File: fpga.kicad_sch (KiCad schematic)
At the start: 33 parts, among them Q1 BSS138PW, SW1 SW_B3U-1000P_SMD, U1 ICE40UP5K-SG48, U3 W25Q32JW_SOIC-8

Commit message: [#72447] Unify capacitors
Signed-off-by: Dawid Lentka <dlentka@antmicro.com>
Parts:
- C1, C2, C3, C4, C5, C6: value C_10u_10V_0402 -> C_10u_0402; symbol antmicroCapacitors0402:C_10u_10V_0402 -> antmicroCapacitors0402:C_10u_0402; MPN GRM155R61A106ME11D -> CC0402MRX5R5BB106; Manufacturer Murata -> YAGEO
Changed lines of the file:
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@@
 	)
 	(symbol
-		(lib_id "antmicroCapacitors0402:C_10u_10V_0402")
+		(lib_id "antmicroCapacitors0402:C_10u_0402")
 		(at 43.18 115.57 90)
 		(unit 1)
@@
 			)
 		)
-		(property "Value" "C_10u_10V_0402"
+		(property "Value" "C_10u_0402"
 			(at 53.34 95.25 0)
 			(effects
@@
 			)
 		)
-		(property "Datasheet" "https://www.murata.com/products/productdetail?partno=GRM155R61A106ME11%23"
+		(property "Datasheet" "https://www.yageo.com/en/Chart/Download/pdf/CC0402MRX5R5BB106"
 			(at 58.42 95.25 0)
 			(effects
@@
 			)
 		)
-		(property "Description" "Multilayer Ceramic Capacitors MLCC - SMD/SMT 10 uF 10 VDC 20% 0402 X5R"
+		(property "Description" "SMD Multilayer Ceramic Capacitor, 10 µF, 6.3 V, 0402 [1005 Metric], ± 20%, X5R, CC Series"
 			(at 43.18 115.57 0)
 			(effects
@@
 			)
 		)
-		(property "MPN" "GRM155R61A106ME11D"
+		(property "MPN" "CC0402MRX5R5BB106"
 			(at 60.96 95.25 0)
 			(effects
@@
 			)
 		)
-		(property "Manufacturer" "Murata"
+		(property "Manufacturer" "YAGEO"
 			(at 63.5 95.25 0)
 			(effects
@@
 	)
 	(symbol
-		(lib_id "antmicroCapacitors0402:C_10u_10V_0402")
+		(lib_id "antmicroCapacitors0402:C_10u_0402")
 		(at 43.18 166.37 90)
 		(unit 1)
@@
 			)
 		)
-		(property "Value" "C_10u_10V_0402"
+		(property "Value" "C_10u_0402"
 			(at 53.34 146.05 0)
 			(effects
@@
 			)
 		)
-		(property "Datasheet" "https://www.murata.com/products/productdetail?partno=GRM155R61A106ME11%23"
+		(property "Datasheet" "https://www.yageo.com/en/Chart/Download/pdf/CC0402MRX5R5BB106"
 			(at 58.42 146.05 0)
 			(effects
@@
 			)
 		)
-		(property "Description" "Multilayer Ceramic Capacitors MLCC - SMD/SMT 10 uF 10 VDC 20% 0402 X5R"
+		(property "Description" "SMD Multilayer Ceramic Capacitor, 10 µF, 6.3 V, 0402 [1005 Metric], ± 20%, X5R, CC Series"
 			(at 43.18 166.37 0)
 			(effects
@@
 			)
 		)
-		(property "MPN" "GRM155R61A106ME11D"
+		(property "MPN" "CC0402MRX5R5BB106"
 			(at 60.96 146.05 0)
 			(effects
@@
 			)
 		)
-		(property "Manufacturer" "Murata"
+		(property "Manufacturer" "YAGEO"
 			(at 63.5 146.05 0)
 			(effects
@@
 	)
 	(symbol
-		(lib_id "antmicroCapacitors0402:C_10u_10V_0402")
+		(lib_id "antmicroCapacitors0402:C_10u_0402")
 		(at 43.18 102.87 90)
 		(unit 1)
@@
 			)
 		)
-		(property "Value" "C_10u_10V_0402"
+		(property "Value" "C_10u_0402"
 			(at 53.34 82.55 0)
 			(effects
@@
 			)
 		)
-		(property "Datasheet" "https://www.murata.com/products/productdetail?partno=GRM155R61A106ME11%23"
+		(property "Datasheet" "https://www.yageo.com/en/Chart/Download/pdf/CC0402MRX5R5BB106"
 			(at 58.42 82.55 0)
 			(effects
@@
 			)
 		)
-		(property "Description" "Multilayer Ceramic Capacitors MLCC - SMD/SMT 10 uF 10 VDC 20% 0402 X5R"
+		(property "Description" "SMD Multilayer Ceramic Capacitor, 10 µF, 6.3 V, 0402 [1005 Metric], ± 20%, X5R, CC Series"
 			(at 43.18 102.87 0)
 			(effects
@@
 			)
 		)
-		(property "MPN" "GRM155R61A106ME11D"
+		(property "MPN" "CC0402MRX5R5BB106"
 			(at 60.96 82.55 0)
 			(effects
@@
 			)
 		)
-		(property "Manufacturer" "Murata"
+		(property "Manufacturer" "YAGEO"
 			(at 63.5 82.55 0)
 			(effects
@@
 	)
 	(symbol
-		(lib_id "antmicroCapacitors0402:C_10u_10V_0402")
+		(lib_id "antmicroCapacitors0402:C_10u_0402")
 		(at 43.18 153.67 90)
 		(unit 1)
@@
 			)
 		)
-		(property "Value" "C_10u_10V_0402"
+		(property "Value" "C_10u_0402"
 			(at 53.34 133.35 0)
 			(effects
@@
 			)
 		)
-		(property "Datasheet" "https://www.murata.com/products/productdetail?partno=GRM155R61A106ME11%23"
+		(property "Datasheet" "https://www.yageo.com/en/Chart/Download/pdf/CC0402MRX5R5BB106"
 			(at 58.42 133.35 0)
 			(effects
@@
 			)
 		)
-		(property "Description" "Multilayer Ceramic Capacitors MLCC - SMD/SMT 10 uF 10 VDC 20% 0402 X5R"
+		(property "Description" "SMD Multilayer Ceramic Capacitor, 10 µF, 6.3 V, 0402 [1005 Metric], ± 20%, X5R, CC Series"
 			(at 43.18 153.67 0)
 			(effects
@@
 			)
 		)
-		(property "MPN" "GRM155R61A106ME11D"
+		(property "MPN" "CC0402MRX5R5BB106"
 			(at 60.96 133.35 0)
 			(effects
@@
 			)
 		)
-		(property "Manufacturer" "Murata"
+		(property "Manufacturer" "YAGEO"
 			(at 63.5 133.35 0)
 			(effects
@@
 	)
 	(symbol
-		(lib_id "antmicroCapacitors0402:C_10u_10V_0402")
+		(lib_id "antmicroCapacitors0402:C_10u_0402")
 		(at 43.18 128.27 90)
 		(unit 1)
@@
 			)
 		)
-		(property "Value" "C_10u_10V_0402"
+		(property "Value" "C_10u_0402"
 			(at 53.34 107.95 0)
 			(effects
@@
 			)
 		)
-		(property "Datasheet" "https://www.murata.com/products/productdetail?partno=GRM155R61A106ME11%23"
+		(property "Datasheet" "https://www.yageo.com/en/Chart/Download/pdf/CC0402MRX5R5BB106"
 			(at 58.42 107.95 0)
 			(effects
@@
 			)
 		)
-		(property "Description" "Multilayer Ceramic Capacitors MLCC - SMD/SMT 10 uF 10 VDC 20% 0402 X5R"
+		(property "Description" "SMD Multilayer Ceramic Capacitor, 10 µF, 6.3 V, 0402 [1005 Metric], ± 20%, X5R, CC Series"
 			(at 43.18 128.27 0)
 			(effects
@@
 			)
 		)
-		(property "MPN" "GRM155R61A106ME11D"
+		(property "MPN" "CC0402MRX5R5BB106"
 			(at 60.96 107.95 0)
 			(effects
@@
 			)
 		)
-		(property "Manufacturer" "Murata"
+		(property "Manufacturer" "YAGEO"
 			(at 63.5 107.95 0)
 			(effects
@@
 	)
 	(symbol
-		(lib_id "antmicroCapacitors0402:C_10u_10V_0402")
+		(lib_id "antmicroCapacitors0402:C_10u_0402")
 		(at 43.18 140.97 90)
 		(unit 1)
@@
 			)
 		)
-		(property "Value" "C_10u_10V_0402"
+		(property "Value" "C_10u_0402"
 			(at 53.34 120.65 0)
 			(effects
@@
 			)
 		)
-		(property "Datasheet" "https://www.murata.com/products/productdetail?partno=GRM155R61A106ME11%23"
+		(property "Datasheet" "https://www.yageo.com/en/Chart/Download/pdf/CC0402MRX5R5BB106"
 			(at 58.42 120.65 0)
 			(effects
@@
 			)
 		)
-		(property "Description" "Multilayer Ceramic Capacitors MLCC - SMD/SMT 10 uF 10 VDC 20% 0402 X5R"
+		(property "Description" "SMD Multilayer Ceramic Capacitor, 10 µF, 6.3 V, 0402 [1005 Metric], ± 20%, X5R, CC Series"
 			(at 43.18 140.97 0)
 			(effects
@@
 			)
 		)
-		(property "MPN" "GRM155R61A106ME11D"
+		(property "MPN" "CC0402MRX5R5BB106"
 			(at 60.96 120.65 0)
 			(effects
@@
 			)
 		)
-		(property "Manufacturer" "Murata"
+		(property "Manufacturer" "YAGEO"
 			(at 63.5 120.65 0)
 			(effects

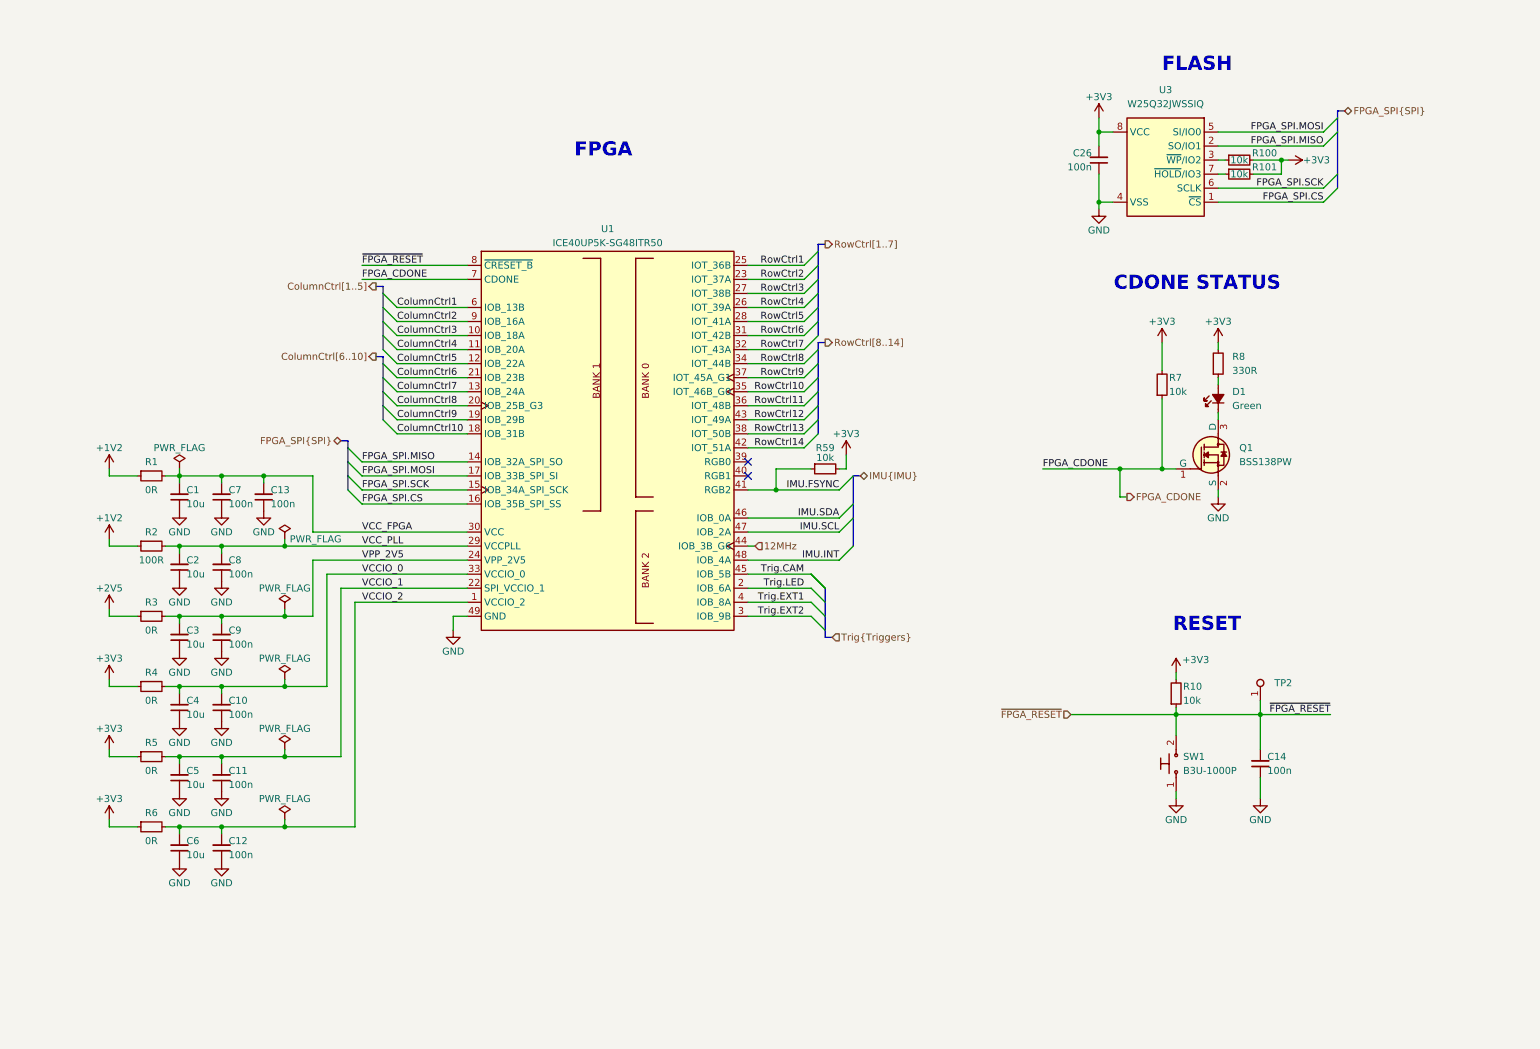
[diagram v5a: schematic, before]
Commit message: [#72447] Update clock & SPI connections
Signed-off-by: Dawid Lentka <dlentka@antmicro.com>
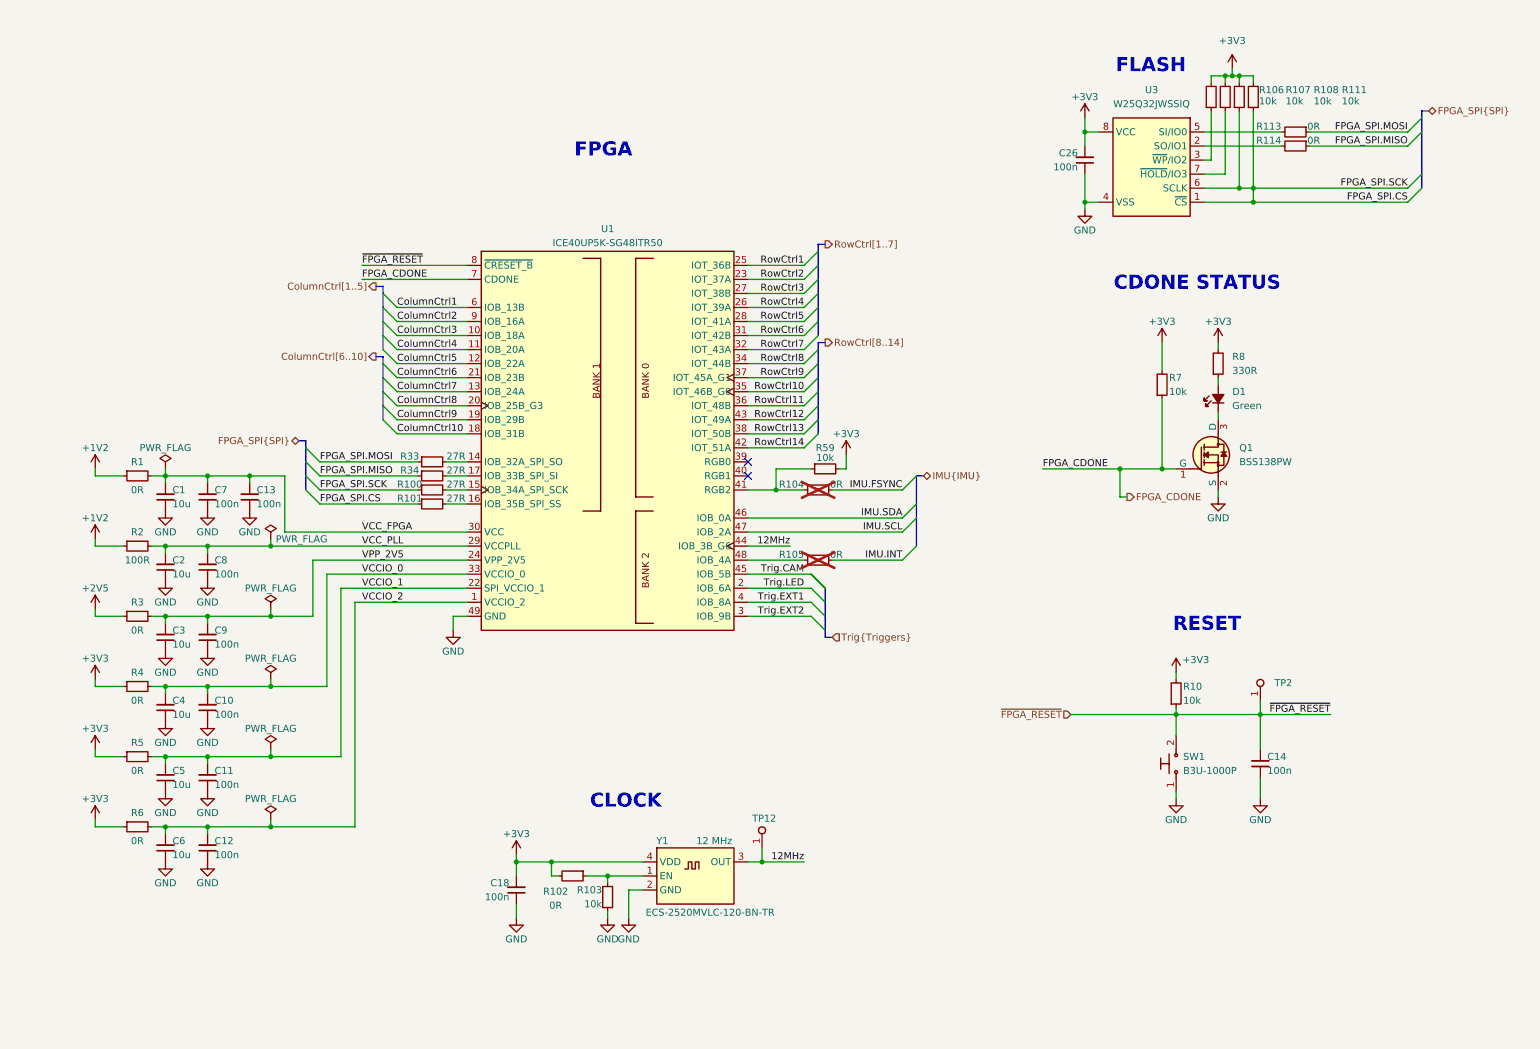
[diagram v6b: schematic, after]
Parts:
- removed R100, R101: R_10k_0402, antmicro-footprints:R_0402_1005Metric, symbol antmicroResistors0402:R_10k_0402
- added C18: C_100n_0402, antmicro-footprints:C_0402_1005Metric, symbol antmicroCapacitors0402:C_100n_0402
- added R100, R101, R33, R34: R_27R_0402, antmicro-footprints:R_0402_1005Metric, symbol antmicroResistors0402:R_27R_0402
- added R102, R104, R105, R113, R114: R_0R_0402, antmicro-footprints:R_0402_1005Metric, symbol antmicroResistors0402:R_0R_0402
- added R103, R106, R107, R108, R111: R_10k_0402, antmicro-footprints:R_0402_1005Metric, symbol antmicroResistors0402:R_10k_0402
- added TP12: TP_0.75mm_SMD, antmicro-footprints:TP_SMD_0.75mm, symbol antmicroTestPoints:TP_0.75mm_SMD
- added Y1: Oscillator_12MHz_ESC_2520MV, antmicro-footprints:Oscillator_SMD_ECS_2520MV_2.5x2mm, symbol antmicroOscillators:Oscillator_12MHz_ESC_2520MV
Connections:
- net +3V3: now also C18.2, R102.2, R106.2, R107.2, R108.2, R111.2, Y1.4 (VDD)
- net 12MHz: now also TP12.1, Y1.3 (OUT)
- net FPGA_SPI.CS: now also U3.6 (SCLK), R100.1, R101.1, R108.1, R111.1; no longer U1.16 (IOB_35B_SPI_SS)
- net FPGA_SPI.MISO: now also R114.1, R34.1; no longer U1.14 (IOB_32A_SPI_SO), U3.2 (SO/IO1)
- net FPGA_SPI.MOSI: now also R113.1, R33.1; no longer U1.17 (IOB_33B_SPI_SI), U3.5 (SI/IO0)
- net GND: now also C18.1, R103.1, Y1.2 (GND)
- net IMU.FSYNC: now also R104.1; no longer R59.1, U1.41 (RGB2)
- net IMU.INT: now also R105.1; no longer U1.48 (IOB_4A)
- net at U3.7 (~{HOLD}/IO3): now also R107.1
- net at U3.3 (~{WP}/IO2): now also R106.1
- net FPGA_SPI.SCK: no longer names the net of U1.15 (IOB_34A_SPI_SCK)
- net FPGA_SPI.SCK: now also R100.2; no longer U3.6 (SCLK)
- new net: R34.2, U1.17 (IOB_33B_SPI_SI)
- new net: R102.1, R103.2, Y1.1 (EN)
- new net: R114.2, U3.2 (SO/IO1)
- new net: R113.2, U3.5 (SI/IO0)
- new net: R33.2, U1.14 (IOB_32A_SPI_SO)
- new net: R104.2, R59.1, U1.41 (RGB2)
- new net: R101.2, U1.16 (IOB_35B_SPI_SS)
- new net: R105.2, U1.48 (IOB_4A)
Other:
- note added: "CLOCK"
- moved on the sheet: C1, C10, C11, C12, C13, C2, C26, C3, C4, C5, C6, C7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

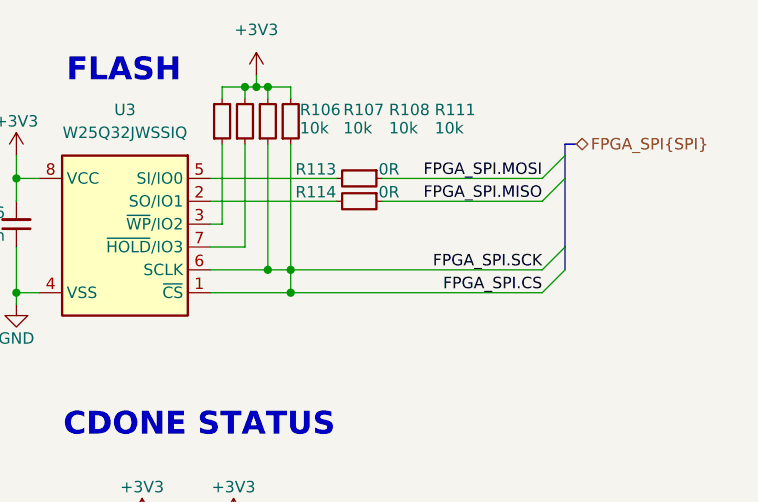
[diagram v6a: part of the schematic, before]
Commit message: [#72447] SCH: remove unwanted junction
Signed-off-by: Dawid Lentka <dlentka@antmicro.com>
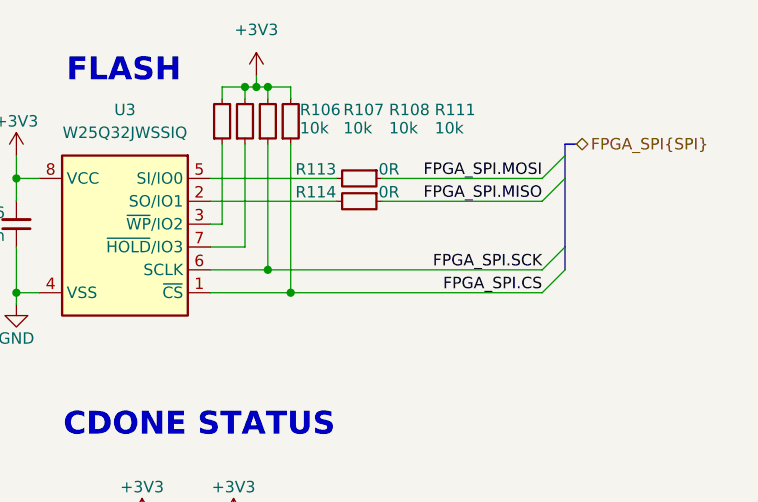
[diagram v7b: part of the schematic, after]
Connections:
- net FPGA_SPI.CS: no longer R100.1, R108.1, U3.6 (SCLK)
- new net FPGA_SPI.SCK: R100.1, R108.1, U3.6 (SCLK)
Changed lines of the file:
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@@
-	)
-	(junction
-		(at 237.49 44.45)
-		(diameter 0)
-		(color 0 0 0 0)
 	)
 	(junction
@@
 	(wire
 		(pts
-			(xy 237.49 44.45) (xy 234.95 44.45)
-		)
-		(stroke
-			(width 0)
-			(type default)
-		)
-	)
-	(wire
-		(pts
 			(xy 59.69 133.35) (xy 59.69 134.62)
 		)
@@
 	(wire
 		(pts
-			(xy 237.49 44.45) (xy 237.49 46.99)
-		)
-		(stroke
-			(width 0)
-			(type default)
-		)
-	)
-	(wire
-		(pts
-			(xy 237.49 30.48) (xy 237.49 44.45)
+			(xy 237.49 30.48) (xy 237.49 46.99)
 		)
 		(stroke
@@
 	(wire
 		(pts
-			(xy 237.49 44.45) (xy 265.43 44.45)
-		)
-		(stroke
+			(xy 234.95 44.45) (xy 265.43 44.45)
+		)
+		(stroke
